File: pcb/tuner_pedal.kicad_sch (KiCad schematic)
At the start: 44 parts, among them J1 Conn_01x04, U1 STM32F411CEUx, U2 PCM1802DB, U3 MCP1700T-3302E/TT, U4 TPS54302, X1 ECS-2520MVLC-081.92, Y1 25MHz 9pF

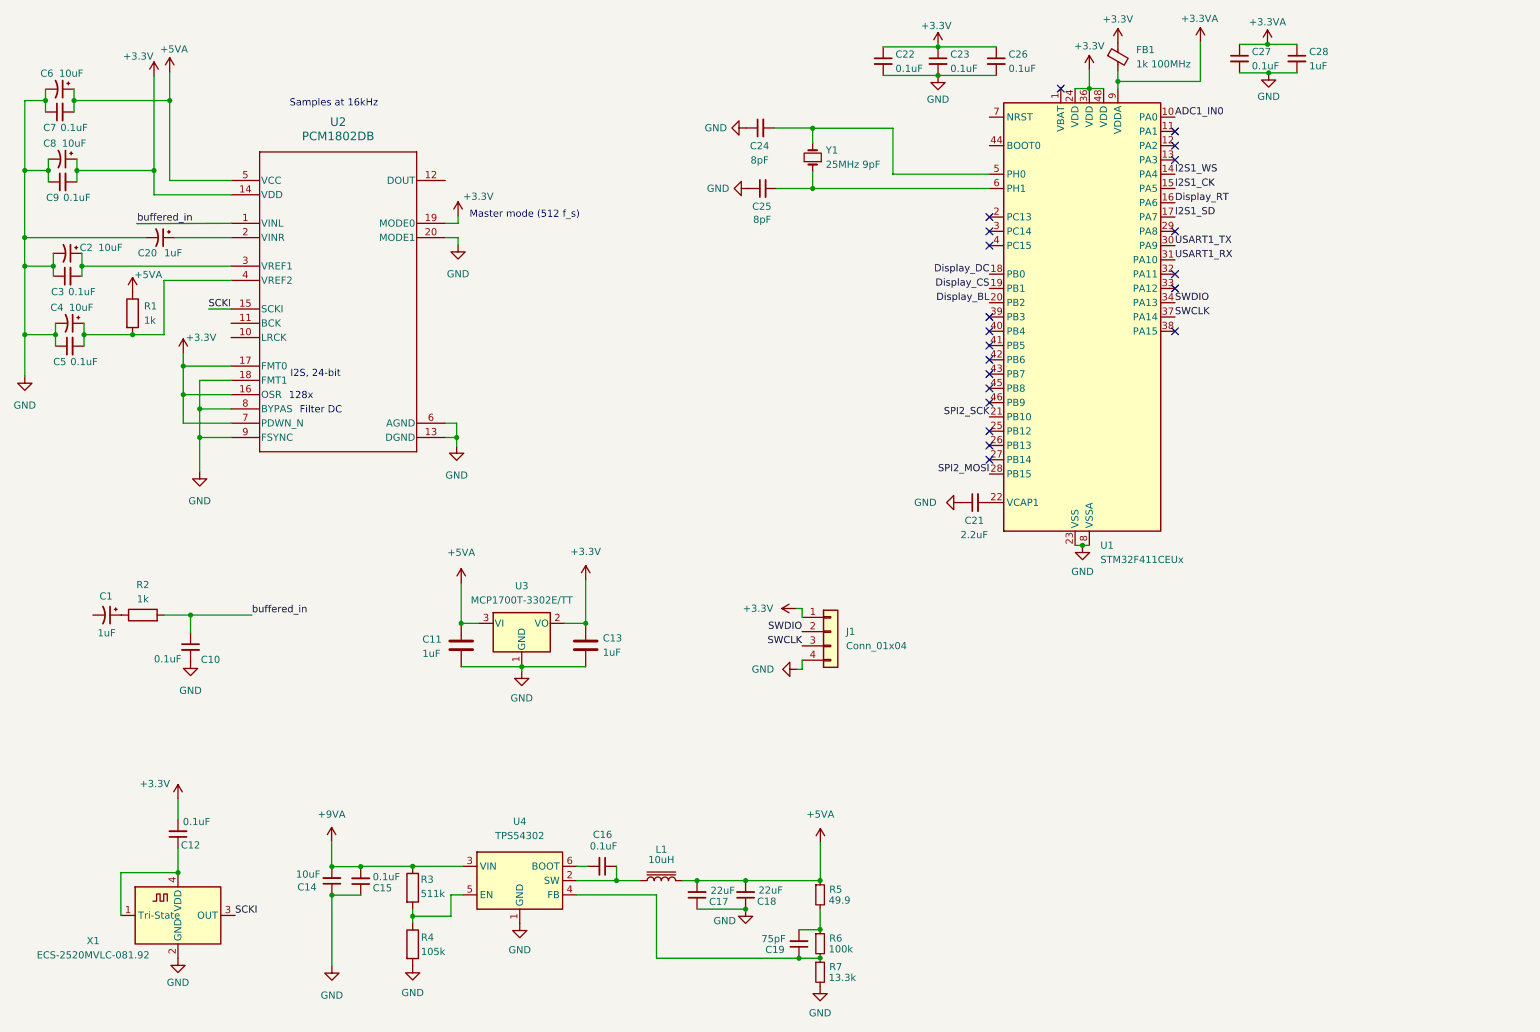
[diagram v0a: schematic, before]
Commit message: Defined headers for each interface
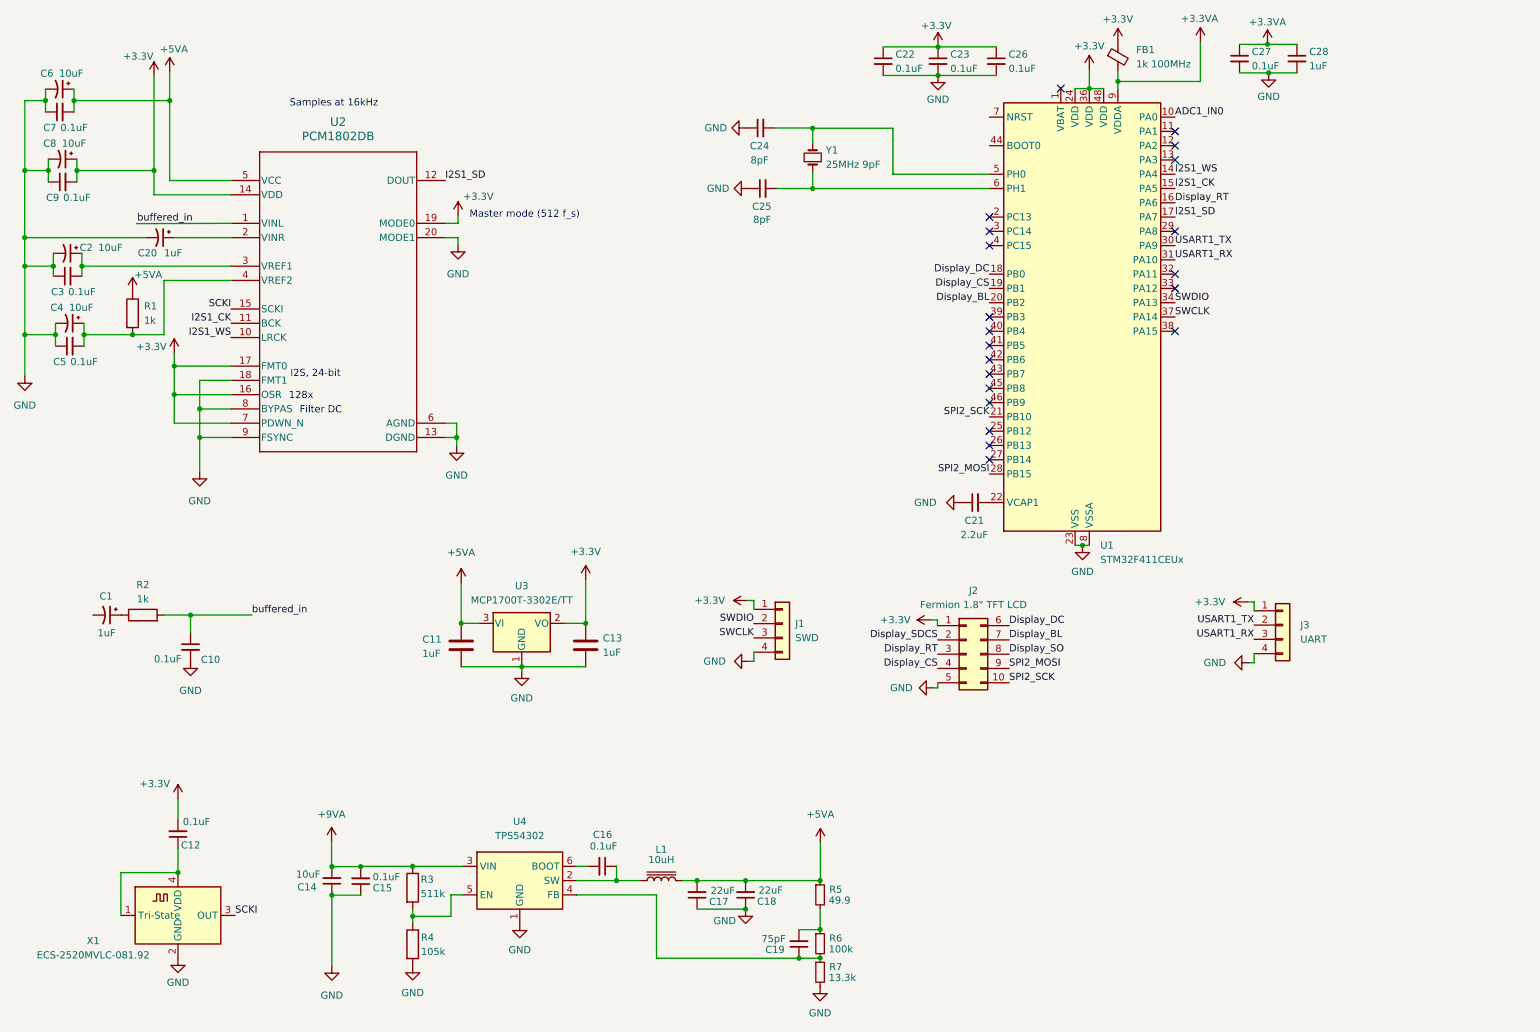
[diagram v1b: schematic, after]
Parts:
- added J2: Fermion 1.8" TFT LCD, Connector_PinHeader_2.54mm:PinHeader_2x05_P2.54mm_Vertical, symbol Connector_Generic:Conn_02x05_Top_Bottom
- added J3: UART, Connector_PinHeader_2.54mm:PinHeader_1x04_P2.54mm_Vertical, symbol Connector_Generic:Conn_01x04
- J1: value Conn_01x04 -> SWD
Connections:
- net +3.3V: now also J2.1 (Pin_1), J3.1 (Pin_1)
- net Display_BL: now also J2.7 (Pin_7)
- net Display_CS: now also J2.4 (Pin_4)
- net Display_DC: now also J2.6 (Pin_6)
- net Display_RT: now also J2.3 (Pin_3)
- net GND: now also J2.5 (Pin_5), J3.4 (Pin_4)
- net I2S1_CK: now also U2.11 (BCK)
- net I2S1_SD: now also U2.12 (DOUT)
- net I2S1_WS: now also U2.10 (LRCK)
- net SPI2_MOSI: now also J2.9 (Pin_9)
- net SPI2_SCK: now also J2.10 (Pin_10)
- net USART1_RX: now also J3.3 (Pin_3)
- net USART1_TX: now also J3.2 (Pin_2)
- new net Display_SDCS: J2.2 (Pin_2)
- new net Display_SO: J2.8 (Pin_8)
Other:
- moved on the sheet: J1

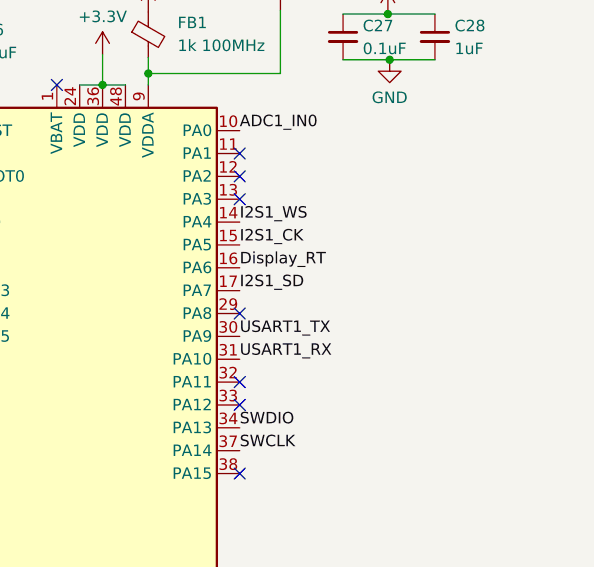
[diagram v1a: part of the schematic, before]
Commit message: Added GPIO attached LED for debugging purposes
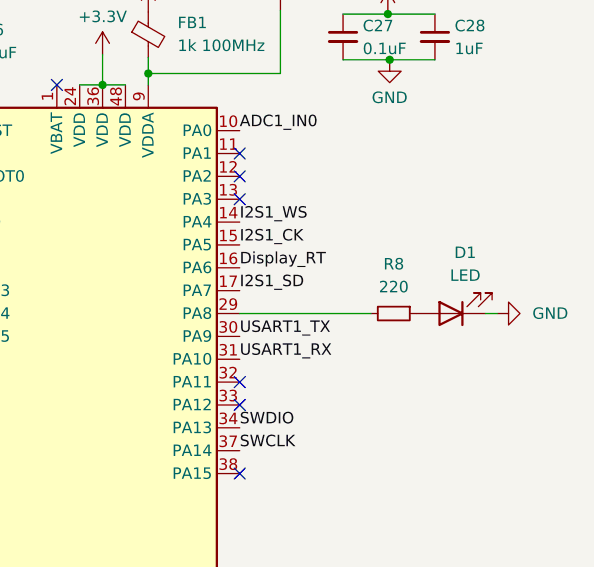
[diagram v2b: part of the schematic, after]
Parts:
- added D1: LED, symbol Device:LED
- added R8: 220, symbol Device:R_Small
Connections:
- net GND: now also D1.1 (K)
- net at U1.29 (PA8): now also R8.2
- new net: D1.2 (A), R8.1
- no-connect marks 21 -> 20
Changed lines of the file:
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@@
   (no_connect (at 191.0588 70.2564))
   (no_connect (at 191.0588 82.9564))
-  (no_connect (at 224.0788 52.4764))
   (no_connect (at 224.0788 70.2564))
   (no_connect (at 224.0788 39.7764))
@@
     (stroke (width 0) (type default))
   )
+  (wire (pts (xy 224.0788 52.4764) (xy 238.6584 52.4764))
+    (stroke (width 0) (type default))
+  )
   (wire (pts (xy 117.6528 167.9956) (xy 124.714 167.9956))
     (stroke (width 0) (type default))
@@
   )
   (wire (pts (xy 29.972 70.866) (xy 29.972 72.898))
+    (stroke (width 0) (type default))
+  )
+  (wire (pts (xy 252.6792 52.4764) (xy 251.3584 52.4764))
     (stroke (width 0) (type default))
   )
@@
         (path "/be09f3cc-c79c-49de-93a4-4a01bf6bfbcf"
           (reference "#PWR018") (unit 1)
+        )
+      )
+    )
+  )
+  (symbol (lib_id "Device:R_Small") (at 241.1984 52.4764 270) (unit 1)
+    (in_bom yes) (on_board yes) (dnp no) (fields_autoplaced)
+    (property "Reference" "R8" (at 241.1984 46.99 90)
+      (effects (font (size 1.27 1.27)))
+    )
+    (property "Value" "220" (at 241.1984 49.53 90)
+      (effects (font (size 1.27 1.27)))
+    )
+    (property "Footprint" "" (at 241.1984 52.4764 0)
+      (effects (font (size 1.27 1.27)) hide)
+    )
+    (property "Datasheet" "~" (at 241.1984 52.4764 0)
+      (effects (font (size 1.27 1.27)) hide)
+    )
+    (pin "1")
+    (pin "2")
+    (instances
+      (project "tuner_pedal"
+        (path "/be09f3cc-c79c-49de-93a4-4a01bf6bfbcf"
+          (reference "R8") (unit 1)
         )
       )
@@
     )
   )
+  (symbol (lib_id "power:GND") (at 252.6792 52.4764 90) (unit 1)
+    (in_bom yes) (on_board yes) (dnp no) (fields_autoplaced)
+    (property "Reference" "#PWR040" (at 259.0292 52.4764 0)
+      (effects (font (size 1.27 1.27)) hide)
+    )
+    (property "Value" "GND" (at 256.5908 52.4764 90)
+      (effects (font (size 1.27 1.27)) (justify right))
+    )
+    (property "Footprint" "" (at 252.6792 52.4764 0)
+      (effects (font (size 1.27 1.27)) hide)
+    )
+    (property "Datasheet" "" (at 252.6792 52.4764 0)
+      (effects (font (size 1.27 1.27)) hide)
+    )
+    (pin "1")
+    (instances
+      (project "tuner_pedal"
+        (path "/be09f3cc-c79c-49de-93a4-4a01bf6bfbcf"
+          (reference "#PWR040") (unit 1)
+        )
+      )
+    )
+  )
   (symbol (lib_id "Device:C_Polarized_Small_US") (at 25.654 27.178 270) (unit 1)
     (in_bom yes) (on_board yes) (dnp no)
@@
         )
       )
+    )
+  )
+  (symbol (lib_id "Device:LED") (at 247.5484 52.4764 180) (unit 1)
+    (in_bom yes) (on_board yes) (dnp no) (fields_autoplaced)
+    (property "Reference" "D1" (at 249.1359 45.72 0)
+      (effects (font (size 1.27 1.27)))
+    )
+    (property "Value" "LED" (at 249.1359 48.26 0)
+      (effects (font (size 1.27 1.27)))
+    )
+    (property "Footprint" "" (at 247.5484 52.4764 0)
+      (effects (font (size 1.27 1.27)) hide)
+    )
+    (property "Datasheet" "~" (at 247.5484 52.4764 0)
+      (effects (font (size 1.27 1.27)) hide)
+    )
+    (pin "1")
+    (pin "2")
+    (instances
+      (project "tuner_pedal"
+        (path "/be09f3cc-c79c-49de-93a4-4a01bf6bfbcf"
+          (reference "D1") (unit 1)
+        )
+      )

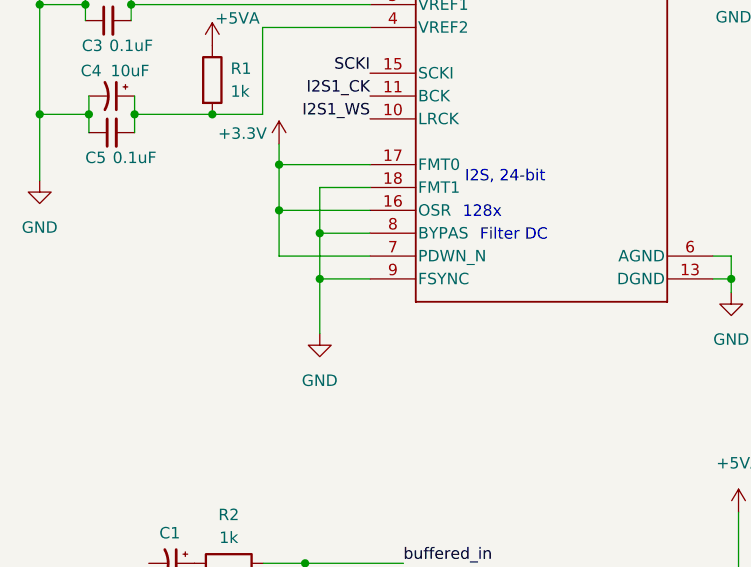
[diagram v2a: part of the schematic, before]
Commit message: Made FSYNC floating
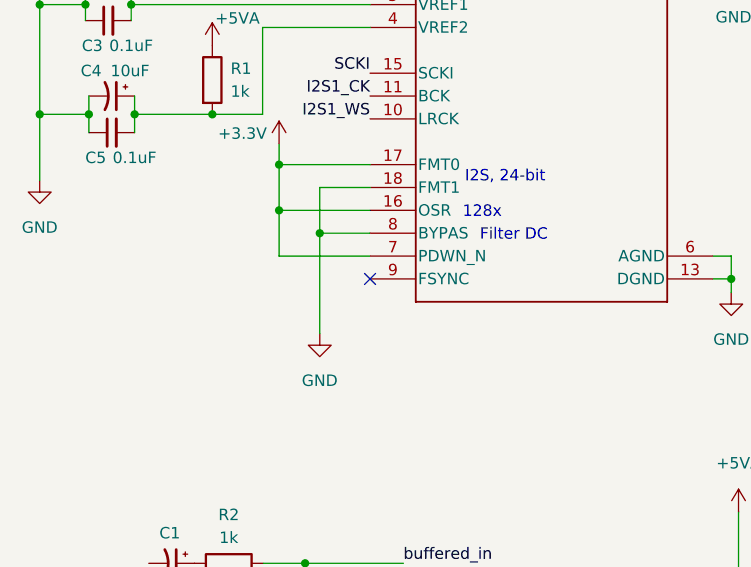
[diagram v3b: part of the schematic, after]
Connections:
- net GND: no longer U2.9 (FSYNC)
- no-connect marks 20 -> 21
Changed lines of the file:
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@@
   (junction (at 147.6756 173.0756) (diameter 0) (color 0 0 0 0)
-  )
-  (junction (at 50.546 89.154) (diameter 0) (color 0 0 0 0)
   )
   (junction (at 19.431 70.866) (diameter 0) (color 0 0 0 0)
@@
   (no_connect (at 191.0588 90.5764))
   (no_connect (at 191.0588 52.4764))
+  (no_connect (at 56.134 89.154))
   (no_connect (at 224.0788 34.6964))
   (no_connect (at 224.0788 62.6364))
@@
     (stroke (width 0) (type default))
   )
-  (wire (pts (xy 50.546 89.154) (xy 50.546 95.25))
-    (stroke (width 0) (type default))
-  )
   (wire (pts (xy 56.134 61.214) (xy 44.196 61.214))
     (stroke (width 0) (type default))
@@
     (stroke (width 0) (type default))
   )
-  (wire (pts (xy 56.134 89.154) (xy 50.546 89.154))
-    (stroke (width 0) (type default))
-  )
   (wire (pts (xy 23.114 29.21) (xy 23.114 31.242))
     (stroke (width 0) (type default))
@@
     (stroke (width 0) (type default))
   )
-  (wire (pts (xy 50.546 84.074) (xy 50.546 89.154))
-    (stroke (width 0) (type default))
-  )
+  (wire (pts (xy 50.546 84.074) (xy 50.546 95.25))
+    (stroke (width 0) (type default))
+  )

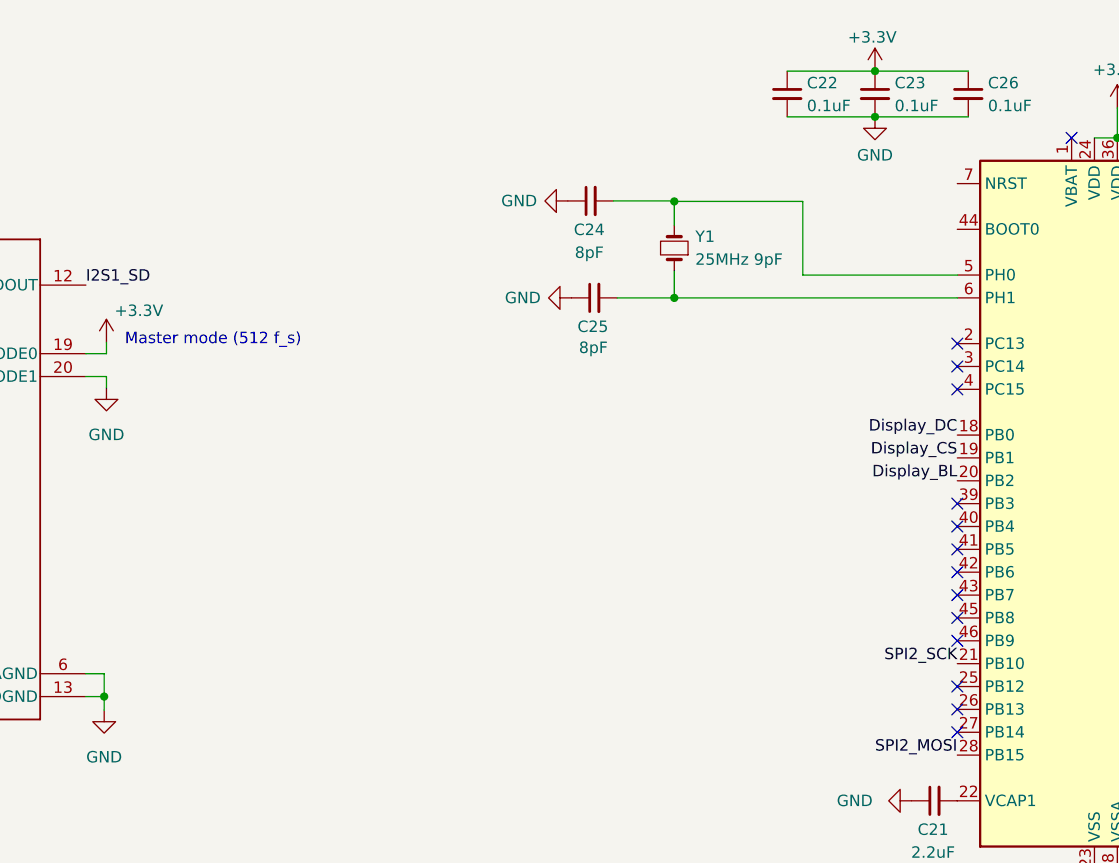
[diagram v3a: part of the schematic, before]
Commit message: Added NRST and BOOT0 buttons
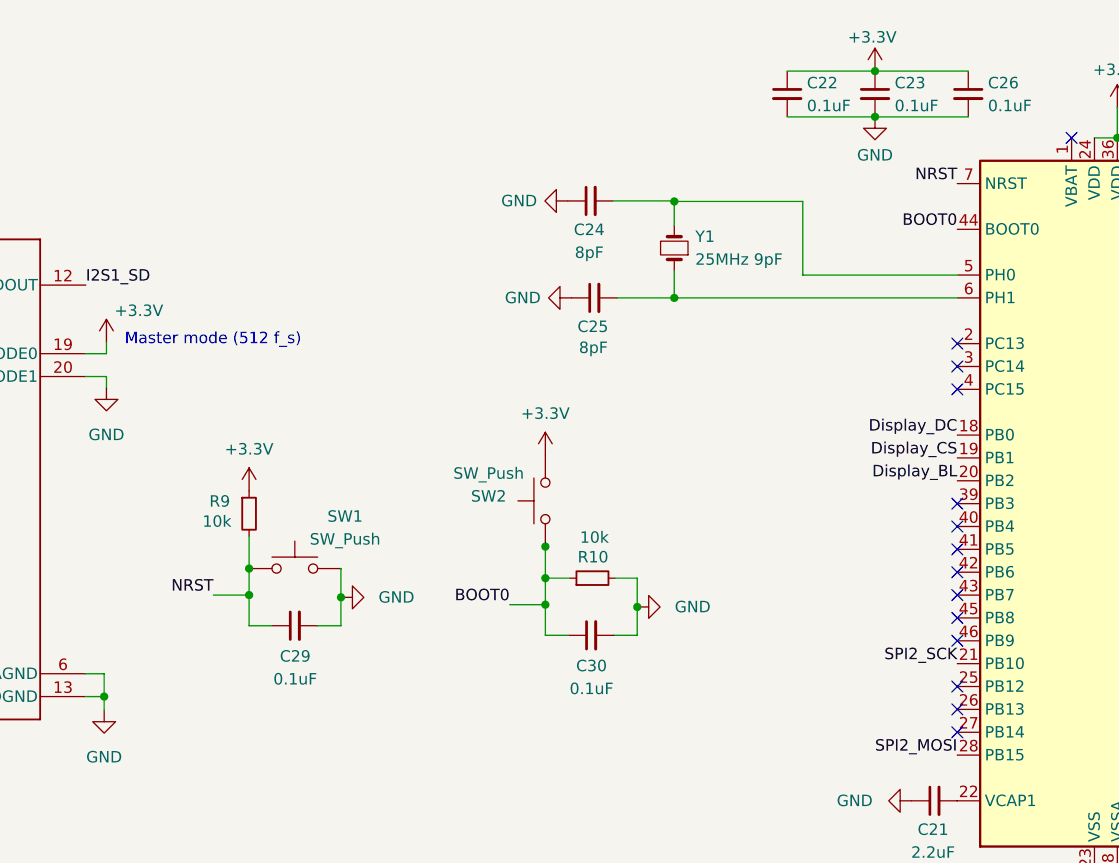
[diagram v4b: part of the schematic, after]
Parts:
- added C29, C30: 0.1uF, symbol Device:C_Small
- added R10, R9: 10k, symbol Device:R_Small
- added SW1, SW2: SW_Push, Button_Switch_SMD:SW_SPST_Omron_B3FS-100xP, symbol Switch:SW_Push
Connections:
- net +3.3V: now also R9.1, SW2.2
- net GND: now also C29.2, C30.2, R10.2, SW1.2
- net BOOT0: now reaches U1.44 (BOOT0)
- net BOOT0: now also C30.1, R10.1, SW2.1
- net NRST: now reaches U1.7 (NRST)
- net NRST: now also C29.1, R9.2, SW1.1
